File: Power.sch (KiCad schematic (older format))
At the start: 15 parts, among them P4 CONN_01X03, U7 TPS799, U9 RT9183

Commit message: added CC1101, fixed mission symbols
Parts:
- C31, C32, C34, C36, C37, C39: footprint (none) -> SFUSat:C_0402
- R11, R12, R5, R6: footprint (none) -> SFUSat:R_0402
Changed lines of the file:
@@
 F 0 "C34" H 5725 2700 50  0000 L CNN
 F 1 "10uF" H 5725 2500 50  0000 L CNN
-F 2 "" H 5738 2450 50  0001 C CNN
+F 2 "SFUSat:C_0402" H 5738 2450 50  0001 C CNN
 F 3 "" H 5700 2600 50  0000 C CNN
 	1    5700 2600
@@
 F 0 "C31" H 5475 2700 50  0000 L CNN
 F 1 "0.1uF" H 5475 2500 50  0000 L CNN
-F 2 "" H 5488 2450 50  0001 C CNN
+F 2 "SFUSat:C_0402" H 5488 2450 50  0001 C CNN
 F 3 "" H 5450 2600 50  0000 C CNN
 	1    5450 2600
@@
 $EndComp
 $Comp
-L GND #PWR043
+L GND #PWR30
 U 1 1 58770941
 P 6900 2800
-F 0 "#PWR043" H 6900 2550 50  0001 C CNN
+F 0 "#PWR30" H 6900 2550 50  0001 C CNN
 F 1 "GND" H 6900 2650 50  0000 C CNN
 F 2 "" H 6900 2800 50  0000 C CNN
@@
 F 0 "C39" H 8075 2700 50  0000 L CNN
 F 1 "10uF" H 8075 2500 50  0000 L CNN
-F 2 "" H 8088 2450 50  0001 C CNN
+F 2 "SFUSat:C_0402" H 8088 2450 50  0001 C CNN
 F 3 "" H 8050 2600 50  0000 C CNN
 	1    8050 2600
@@
 $EndComp
 $Comp
-L GND #PWR044
+L GND #PWR34
 U 1 1 58770B93
 P 8050 2750
-F 0 "#PWR044" H 8050 2500 50  0001 C CNN
+F 0 "#PWR34" H 8050 2500 50  0001 C CNN
 F 1 "GND" H 8050 2600 50  0000 C CNN
 F 2 "" H 8050 2750 50  0000 C CNN
@@
 $EndComp
 $Comp
-L GND #PWR045
+L GND #PWR33
 U 1 1 58770BD7
 P 7650 2750
-F 0 "#PWR045" H 7650 2500 50  0001 C CNN
+F 0 "#PWR33" H 7650 2500 50  0001 C CNN
 F 1 "GND" H 7650 2600 50  0000 C CNN
 F 2 "" H 7650 2750 50  0000 C CNN
@@
 $EndComp
 $Comp
-L GND #PWR046
+L GND #PWR28
 U 1 1 58770CCB
 P 5700 2750
-F 0 "#PWR046" H 5700 2500 50  0001 C CNN
+F 0 "#PWR28" H 5700 2500 50  0001 C CNN
 F 1 "GND" H 5700 2600 50  0000 C CNN
 F 2 "" H 5700 2750 50  0000 C CNN
@@
 $EndComp
 $Comp
-L GND #PWR047
+L GND #PWR26
 U 1 1 58770CE7
 P 5450 2750
-F 0 "#PWR047" H 5450 2500 50  0001 C CNN
+F 0 "#PWR26" H 5450 2500 50  0001 C CNN
 F 1 "GND" H 5450 2600 50  0000 C CNN
 F 2 "" H 5450 2750 50  0000 C CNN
@@
 F 0 "R12" V 7730 2550 50  0000 C CNN
 F 1 "286" V 7650 2550 50  0000 C CNN
-F 2 "" V 7580 2550 50  0001 C CNN
+F 2 "SFUSat:R_0402" V 7580 2550 50  0001 C CNN
 F 3 "" H 7650 2550 50  0000 C CNN
 	1    7650 2550
@@
 F 0 "R11" H 7730 2150 50  0000 C CNN
 F 1 "1k" V 7650 2150 50  0000 C CNN
-F 2 "" V 7580 2150 50  0001 C CNN
+F 2 "SFUSat:R_0402" V 7580 2150 50  0001 C CNN
 F 3 "" H 7650 2150 50  0000 C CNN
 	1    7650 2150
@@
 $EndComp
 $Comp
-L GND #PWR048
+L GND #PWR29
 U 1 1 5879D9E2
 P 6350 4000
-F 0 "#PWR048" H 6350 3750 50  0001 C CNN
+F 0 "#PWR29" H 6350 3750 50  0001 C CNN
 F 1 "GND" H 6350 3850 50  0000 C CNN
 F 2 "" H 6350 4000 50  0000 C CNN
@@
 $EndComp
 $Comp
-L GND #PWR049
+L GND #PWR32
 U 1 1 5879DA04
 P 7150 4000
-F 0 "#PWR049" H 7150 3750 50  0001 C CNN
+F 0 "#PWR32" H 7150 3750 50  0001 C CNN
 F 1 "GND" H 7150 3850 50  0000 C CNN
 F 2 "" H 7150 4000 50  0000 C CNN
@@
 $EndComp
 $Comp
-L GND #PWR050
+L GND #PWR31
 U 1 1 5879DA26
 P 6950 4000
-F 0 "#PWR050" H 6950 3750 50  0001 C CNN
+F 0 "#PWR31" H 6950 3750 50  0001 C CNN
 F 1 "GND" H 6950 3850 50  0000 C CNN
 F 2 "" H 6950 4000 50  0000 C CNN
@@
 F 0 "C36" H 6975 3950 50  0000 L CNN
 F 1 "DNP" H 6975 3750 50  0000 L CNN
-F 2 "" H 6988 3700 50  0001 C CNN
+F 2 "SFUSat:C_0402" H 6988 3700 50  0001 C CNN
 F 3 "" H 6950 3850 50  0000 C CNN
 	1    6950 3850
@@
 F 0 "C37" H 7175 3950 50  0000 L CNN
 F 1 "2.2uF" H 7175 3750 50  0000 L CNN
-F 2 "" H 7188 3700 50  0001 C CNN
+F 2 "SFUSat:C_0402" H 7188 3700 50  0001 C CNN
 F 3 "" H 7150 3850 50  0000 C CNN
 	1    7150 3850
@@
 $EndComp
 $Comp
-L GND #PWR051
+L GND #PWR27
 U 1 1 5879E264
 P 5550 4000
-F 0 "#PWR051" H 5550 3750 50  0001 C CNN
+F 0 "#PWR27" H 5550 3750 50  0001 C CNN
 F 1 "GND" H 5550 3850 50  0000 C CNN
 F 2 "" H 5550 4000 50  0000 C CNN
@@
 F 0 "C32" H 5575 3950 50  0000 L CNN
 F 1 "0.1uF" H 5575 3750 50  0000 L CNN
-F 2 "" H 5588 3700 50  0001 C CNN
+F 2 "SFUSat:C_0402" H 5588 3700 50  0001 C CNN
 F 3 "" H 5550 3850 50  0000 C CNN
 	1    5550 3850
@@
 F 0 "R6" V 6130 2150 50  0000 C CNN
 F 1 "1k" V 6050 2150 50  0000 C CNN
-F 2 "" V 5980 2150 50  0001 C CNN
+F 2 "SFUSat:R_0402" V 5980 2150 50  0001 C CNN
 F 3 "" H 6050 2150 50  0000 C CNN
 	1    6050 2150
@@
 F 0 "R5" V 5805 3500 50  0000 C CNN
 F 1 "1k" V 5725 3500 50  0000 C CNN
-F 2 "" V 5655 3500 50  0001 C CNN
+F 2 "SFUSat:R_0402" V 5655 3500 50  0001 C CNN
 F 3 "" H 5725 3500 50  0000 C CNN
 	1    5725 3500

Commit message: fixed rescue library
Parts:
- P4: footprint (none) -> SFUSat:Socket_Strip_Straight_1x03
- U7: footprint (none) -> SFUSat:SOT-363
- U9: footprint (none) -> SFUSat:TO-263-5Lead
- W4, W5: footprint (none) -> SFUSat:EXPOSED
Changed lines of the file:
@@
 EESchema Schematic File Version 2
-LIBS:SFUSat-Radio-rescue
 LIBS:power
 LIBS:device
@@
 F 0 "U9" H 7200 2450 60  0000 C CNN
 F 1 "RT9183" H 6900 2150 60  0000 C CNN
-F 2 "" H 6900 2150 60  0001 C CNN
+F 2 "SFUSat:TO-263-5Lead" H 6900 2150 60  0001 C CNN
 F 3 "" H 6900 2150 60  0001 C CNN
 	1    6900 2150
@@
 $EndComp
 $Comp
-L GND #PWR30
+L GND #PWR030
 U 1 1 58770941
 P 6900 2800
-F 0 "#PWR30" H 6900 2550 50  0001 C CNN
+F 0 "#PWR030" H 6900 2550 50  0001 C CNN
 F 1 "GND" H 6900 2650 50  0000 C CNN
 F 2 "" H 6900 2800 50  0000 C CNN
@@
 $EndComp
 $Comp
-L GND #PWR34
+L GND #PWR031
 U 1 1 58770B93
 P 8050 2750
-F 0 "#PWR34" H 8050 2500 50  0001 C CNN
+F 0 "#PWR031" H 8050 2500 50  0001 C CNN
 F 1 "GND" H 8050 2600 50  0000 C CNN
 F 2 "" H 8050 2750 50  0000 C CNN
@@
 $EndComp
 $Comp
-L GND #PWR33
+L GND #PWR032
 U 1 1 58770BD7
 P 7650 2750
-F 0 "#PWR33" H 7650 2500 50  0001 C CNN
+F 0 "#PWR032" H 7650 2500 50  0001 C CNN
 F 1 "GND" H 7650 2600 50  0000 C CNN
 F 2 "" H 7650 2750 50  0000 C CNN
@@
 $EndComp
 $Comp
-L GND #PWR28
+L GND #PWR033
 U 1 1 58770CCB
 P 5700 2750
-F 0 "#PWR28" H 5700 2500 50  0001 C CNN
+F 0 "#PWR033" H 5700 2500 50  0001 C CNN
 F 1 "GND" H 5700 2600 50  0000 C CNN
 F 2 "" H 5700 2750 50  0000 C CNN
@@
 $EndComp
 $Comp
-L GND #PWR26
+L GND #PWR034
 U 1 1 58770CE7
 P 5450 2750
-F 0 "#PWR26" H 5450 2500 50  0001 C CNN
+F 0 "#PWR034" H 5450 2500 50  0001 C CNN
 F 1 "GND" H 5450 2600 50  0000 C CNN
 F 2 "" H 5450 2750 50  0000 C CNN
@@
 F 0 "U7" H 6600 3700 60  0000 C CNN
 F 1 "TPS799" H 6350 3450 60  0000 C CNN
-F 2 "" H 6350 3450 60  0001 C CNN
+F 2 "SFUSat:SOT-363" H 6350 3450 60  0001 C CNN
 F 3 "" H 6350 3450 60  0001 C CNN
 	1    6350 3450
@@
 $EndComp
 $Comp
-L GND #PWR29
+L GND #PWR035
 U 1 1 5879D9E2
 P 6350 4000
-F 0 "#PWR29" H 6350 3750 50  0001 C CNN
+F 0 "#PWR035" H 6350 3750 50  0001 C CNN
 F 1 "GND" H 6350 3850 50  0000 C CNN
 F 2 "" H 6350 4000 50  0000 C CNN
@@
 $EndComp
 $Comp
-L GND #PWR32
+L GND #PWR036
 U 1 1 5879DA04
 P 7150 4000
-F 0 "#PWR32" H 7150 3750 50  0001 C CNN
+F 0 "#PWR036" H 7150 3750 50  0001 C CNN
 F 1 "GND" H 7150 3850 50  0000 C CNN
 F 2 "" H 7150 4000 50  0000 C CNN
@@
 $EndComp
 $Comp
-L GND #PWR31
+L GND #PWR037
 U 1 1 5879DA26
 P 6950 4000
-F 0 "#PWR31" H 6950 3750 50  0001 C CNN
+F 0 "#PWR037" H 6950 3750 50  0001 C CNN
 F 1 "GND" H 6950 3850 50  0000 C CNN
 F 2 "" H 6950 4000 50  0000 C CNN
@@
 $EndComp
 $Comp
-L GND #PWR27
+L GND #PWR038
 U 1 1 5879E264
 P 5550 4000
-F 0 "#PWR27" H 5550 3750 50  0001 C CNN
+F 0 "#PWR038" H 5550 3750 50  0001 C CNN
 F 1 "GND" H 5550 3850 50  0000 C CNN
 F 2 "" H 5550 4000 50  0000 C CNN
@@
 F 0 "P4" H 3700 4300 50  0000 C CNN
 F 1 "CONN_01X03" V 3800 4100 50  0000 C CNN
-F 2 "" H 3700 4100 50  0001 C CNN
+F 2 "SFUSat:Socket_Strip_Straight_1x03" H 3700 4100 50  0001 C CNN
 F 3 "" H 3700 4100 50  0000 C CNN
 	1    3700 4100
@@
 F 0 "W4" H 3050 4870 50  0000 C CNN
 F 1 "TEST_1P" H 3050 4800 50  0000 C CNN
-F 2 "" H 3250 4600 50  0001 C CNN
+F 2 "SFUSat:EXPOSED" H 3250 4600 50  0001 C CNN
 F 3 "" H 3250 4600 50  0000 C CNN
 	1    3050 4600
@@
 F 0 "W5" H 3050 5070 50  0000 C CNN
 F 1 "TEST_1P" H 3050 5000 50  0000 C CNN
-F 2 "" H 3250 4800 50  0001 C CNN
+F 2 "SFUSat:EXPOSED" H 3250 4800 50  0001 C CNN
 F 3 "" H 3250 4800 50  0000 C CNN
 	1    3050 4800

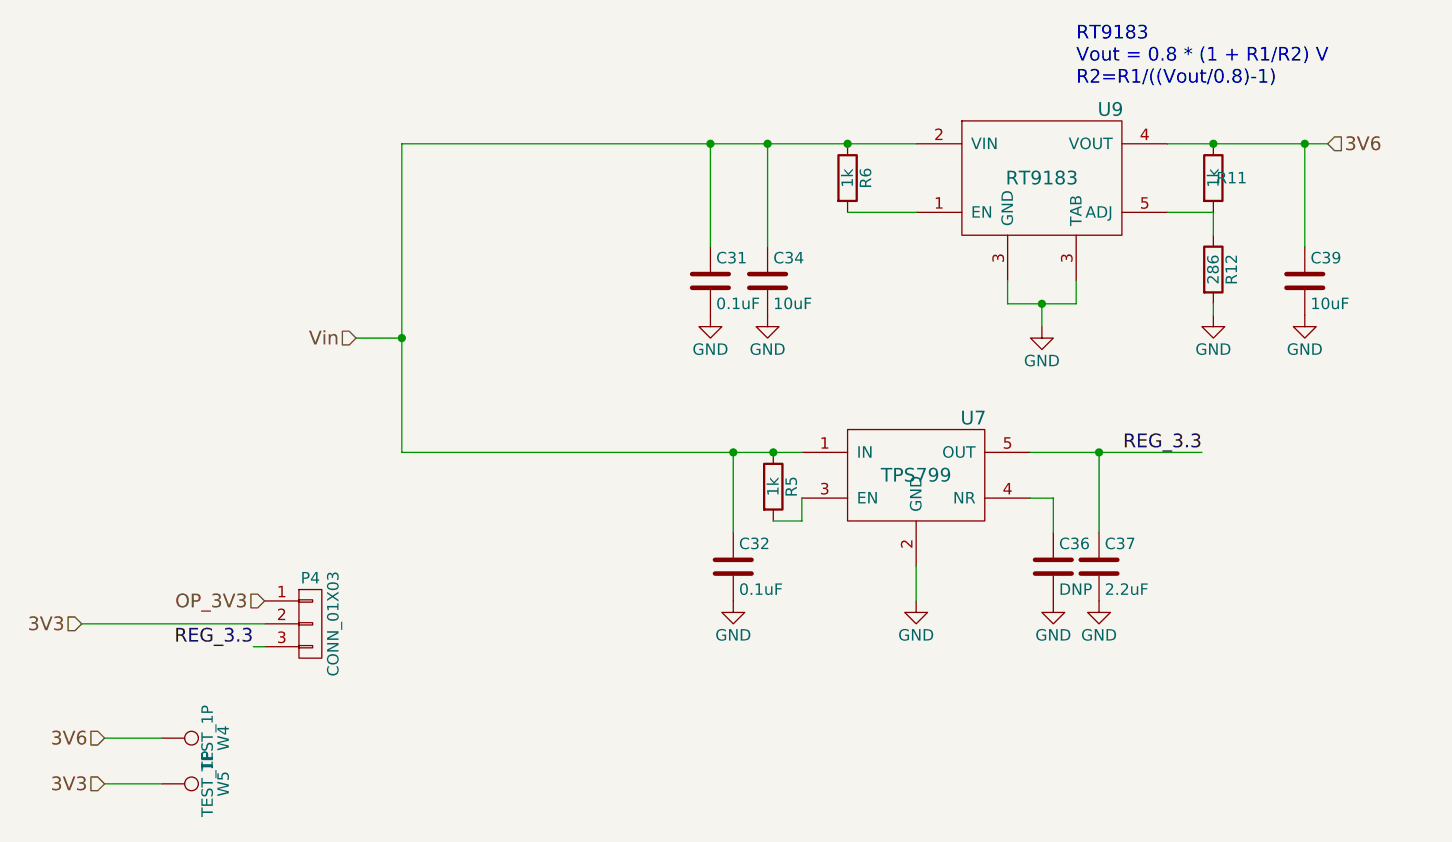
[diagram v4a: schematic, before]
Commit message: Renumbered reference designators
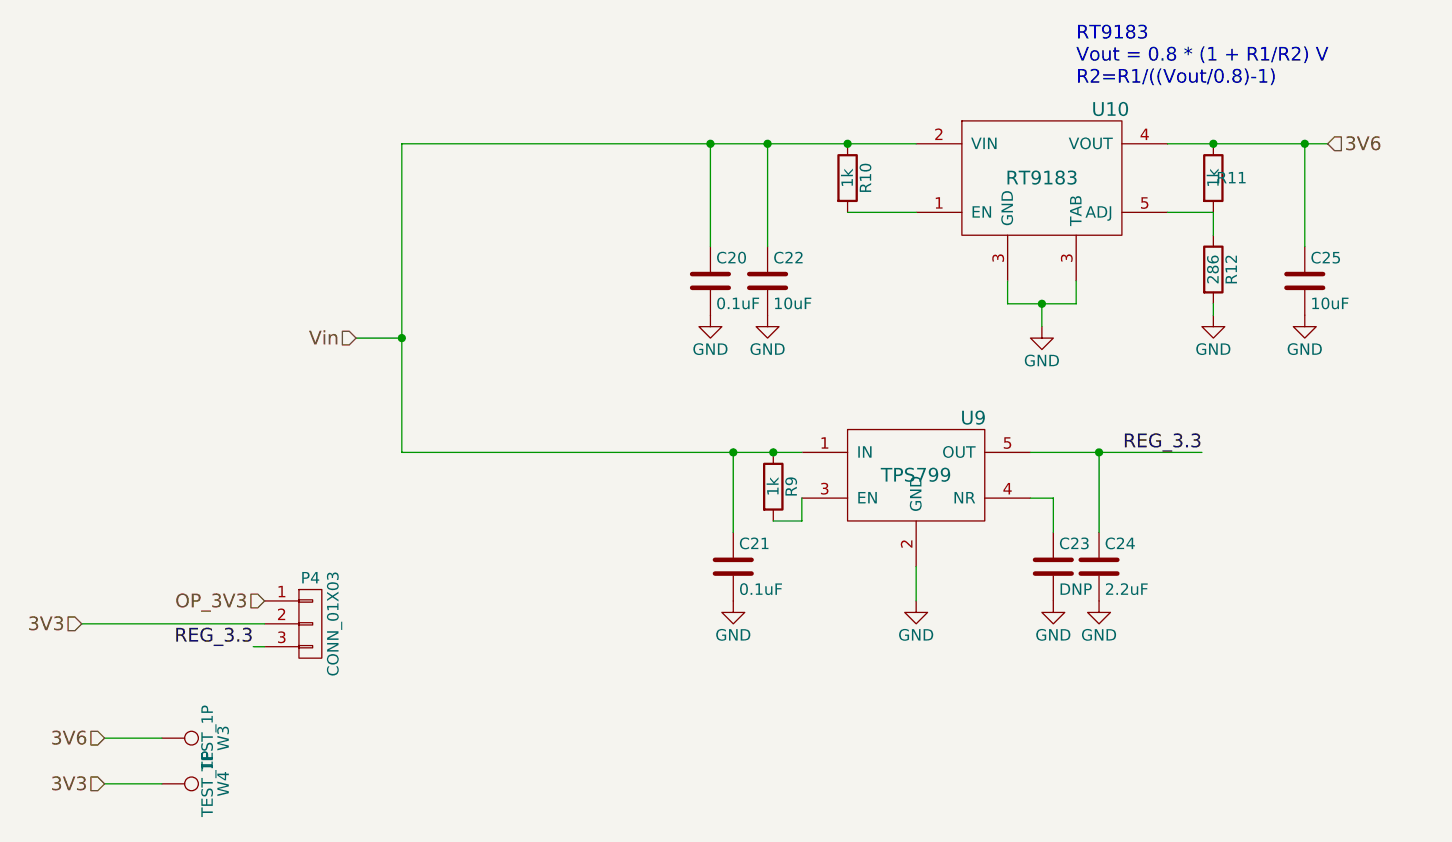
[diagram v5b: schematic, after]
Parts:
- renumbered C31 to C20, C32 to C21, C34 to C22, C36 to C23, C37 to C24, C39 to C25, R6 to R10, R5 to R9, U9 to U10, U7 to U9, W4 to W3, W5 to W4
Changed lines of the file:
@@
 3V6
 $Comp
-L RT9183 U9
+L RT9183 U10
 U 1 1 58770580
 P 6900 2150
-F 0 "U9" H 7200 2450 60  0000 C CNN
+F 0 "U10" H 7200 2450 60  0000 C CNN
 F 1 "RT9183" H 6900 2150 60  0000 C CNN
 F 2 "SFUSat:TO-263-5Lead" H 6900 2150 60  0001 C CNN
@@
 $EndComp
 $Comp
-L C C34
+L C C22
 U 1 1 587706B0
 P 5700 2600
-F 0 "C34" H 5725 2700 50  0000 L CNN
+F 0 "C22" H 5725 2700 50  0000 L CNN
 F 1 "10uF" H 5725 2500 50  0000 L CNN
 F 2 "SFUSat:C_0402" H 5738 2450 50  0001 C CNN
@@
 $EndComp
 $Comp
-L C C31
+L C C20
 U 1 1 58770789
 P 5450 2600
-F 0 "C31" H 5475 2700 50  0000 L CNN
+F 0 "C20" H 5475 2700 50  0000 L CNN
 F 1 "0.1uF" H 5475 2500 50  0000 L CNN
 F 2 "SFUSat:C_0402" H 5488 2450 50  0001 C CNN
@@
 $EndComp
 $Comp
-L GND #PWR037
+L GND #PWR036
 U 1 1 58770941
 P 6900 2800
-F 0 "#PWR037" H 6900 2550 50  0001 C CNN
+F 0 "#PWR036" H 6900 2550 50  0001 C CNN
 F 1 "GND" H 6900 2650 50  0000 C CNN
 F 2 "" H 6900 2800 50  0000 C CNN
@@
 $EndComp
 $Comp
-L C C39
+L C C25
 U 1 1 58770AC4
 P 8050 2600
-F 0 "C39" H 8075 2700 50  0000 L CNN
+F 0 "C25" H 8075 2700 50  0000 L CNN
 F 1 "10uF" H 8075 2500 50  0000 L CNN
 F 2 "SFUSat:C_0402" H 8088 2450 50  0001 C CNN
@@
 $EndComp
 $Comp
-L GND #PWR038
+L GND #PWR037
 U 1 1 58770B93
 P 8050 2750
-F 0 "#PWR038" H 8050 2500 50  0001 C CNN
+F 0 "#PWR037" H 8050 2500 50  0001 C CNN
 F 1 "GND" H 8050 2600 50  0000 C CNN
 F 2 "" H 8050 2750 50  0000 C CNN
@@
 $EndComp
 $Comp
-L GND #PWR039
+L GND #PWR038
 U 1 1 58770BD7
 P 7650 2750
-F 0 "#PWR039" H 7650 2500 50  0001 C CNN
+F 0 "#PWR038" H 7650 2500 50  0001 C CNN
 F 1 "GND" H 7650 2600 50  0000 C CNN
 F 2 "" H 7650 2750 50  0000 C CNN
@@
 $EndComp
 $Comp
-L GND #PWR040
+L GND #PWR039
 U 1 1 58770CCB
 P 5700 2750
-F 0 "#PWR040" H 5700 2500 50  0001 C CNN
+F 0 "#PWR039" H 5700 2500 50  0001 C CNN
 F 1 "GND" H 5700 2600 50  0000 C CNN
 F 2 "" H 5700 2750 50  0000 C CNN
@@
 $EndComp
 $Comp
-L GND #PWR041
+L GND #PWR040
 U 1 1 58770CE7
 P 5450 2750
-F 0 "#PWR041" H 5450 2500 50  0001 C CNN
+F 0 "#PWR040" H 5450 2500 50  0001 C CNN
 F 1 "GND" H 5450 2600 50  0000 C CNN
 F 2 "" H 5450 2750 50  0000 C CNN
@@
 RT9183\nVout = 0.8 * (1 + R1/R2) V\nR2=R1/((Vout/0.8)-1)
 $Comp
-L TPS799 U7
+L TPS799 U9
 U 1 1 5879CF29
 P 6350 3450
-F 0 "U7" H 6600 3700 60  0000 C CNN
+F 0 "U9" H 6600 3700 60  0000 C CNN
 F 1 "TPS799" H 6350 3450 60  0000 C CNN
 F 2 "SFUSat:SOT-363" H 6350 3450 60  0001 C CNN
@@
 $EndComp
 $Comp
-L GND #PWR042
+L GND #PWR041
 U 1 1 5879D9E2
 P 6350 4000
-F 0 "#PWR042" H 6350 3750 50  0001 C CNN
+F 0 "#PWR041" H 6350 3750 50  0001 C CNN
 F 1 "GND" H 6350 3850 50  0000 C CNN
 F 2 "" H 6350 4000 50  0000 C CNN
@@
 $EndComp
 $Comp
-L GND #PWR043
+L GND #PWR042
 U 1 1 5879DA04
 P 7150 4000
-F 0 "#PWR043" H 7150 3750 50  0001 C CNN
+F 0 "#PWR042" H 7150 3750 50  0001 C CNN
 F 1 "GND" H 7150 3850 50  0000 C CNN
 F 2 "" H 7150 4000 50  0000 C CNN
@@
 $EndComp
 $Comp
-L GND #PWR044
+L GND #PWR043
 U 1 1 5879DA26
 P 6950 4000
-F 0 "#PWR044" H 6950 3750 50  0001 C CNN
+F 0 "#PWR043" H 6950 3750 50  0001 C CNN
 F 1 "GND" H 6950 3850 50  0000 C CNN
 F 2 "" H 6950 4000 50  0000 C CNN
@@
 $EndComp
 $Comp
-L C C36
+L C C23
 U 1 1 5879DA48
 P 6950 3850
-F 0 "C36" H 6975 3950 50  0000 L CNN
+F 0 "C23" H 6975 3950 50  0000 L CNN
 F 1 "DNP" H 6975 3750 50  0000 L CNN
 F 2 "SFUSat:C_0402" H 6988 3700 50  0001 C CNN
@@
 $EndComp
 $Comp
-L C C37
+L C C24
 U 1 1 5879DAAB
 P 7150 3850
-F 0 "C37" H 7175 3950 50  0000 L CNN
+F 0 "C24" H 7175 3950 50  0000 L CNN
 F 1 "2.2uF" H 7175 3750 50  0000 L CNN
 F 2 "SFUSat:C_0402" H 7188 3700 50  0001 C CNN
@@
 $EndComp
 $Comp
-L GND #PWR045
+L GND #PWR044
 U 1 1 5879E264
 P 5550 4000
-F 0 "#PWR045" H 5550 3750 50  0001 C CNN
+F 0 "#PWR044" H 5550 3750 50  0001 C CNN
 F 1 "GND" H 5550 3850 50  0000 C CNN
 F 2 "" H 5550 4000 50  0000 C CNN
@@
 $EndComp
 $Comp
-L C C32
+L C C21
 U 1 1 5879E323
 P 5550 3850
-F 0 "C32" H 5575 3950 50  0000 L CNN
+F 0 "C21" H 5575 3950 50  0000 L CNN
 F 1 "0.1uF" H 5575 3750 50  0000 L CNN
 F 2 "SFUSat:C_0402" H 5588 3700 50  0001 C CNN
@@
 3V3
 $Comp
-L TEST_1P W4
+L TEST_1P W3
 U 1 1 588228DF
 P 3050 4600
-F 0 "W4" H 3050 4870 50  0000 C CNN
+F 0 "W3" H 3050 4870 50  0000 C CNN
 F 1 "TEST_1P" H 3050 4800 50  0000 C CNN
 F 2 "SFUSat:EXPOSED" H 3250 4600 50  0001 C CNN
@@
 $EndComp
 $Comp
-L TEST_1P W5
+L TEST_1P W4
 U 1 1 58822942
 P 3050 4800
-F 0 "W5" H 3050 5070 50  0000 C CNN
+F 0 "W4" H 3050 5070 50  0000 C CNN
 F 1 "TEST_1P" H 3050 5000 50  0000 C CNN
 F 2 "SFUSat:EXPOSED" H 3250 4800 50  0001 C CNN
@@
 $EndComp
 $Comp
-L R R6
+L R R10
 U 1 1 58948617
 P 6050 2150
-F 0 "R6" V 6130 2150 50  0000 C CNN
+F 0 "R10" V 6130 2150 50  0000 C CNN
 F 1 "1k" V 6050 2150 50  0000 C CNN
 F 2 "SFUSat:R_0402" V 5980 2150 50  0001 C CNN
@@
 $EndComp
 $Comp
-L R R5
+L R R9
 U 1 1 58948796
 P 5725 3500
-F 0 "R5" V 5805 3500 50  0000 C CNN
+F 0 "R9" V 5805 3500 50  0000 C CNN
 F 1 "1k" V 5725 3500 50  0000 C CNN
 F 2 "SFUSat:R_0402" V 5655 3500 50  0001 C CNN
